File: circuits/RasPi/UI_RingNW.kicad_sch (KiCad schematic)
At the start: 11 parts, among them SW2 SW_DIP_x04, SW3 SW_SPDT

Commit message: ラズパイ基板とか
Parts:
- R4, R5: value 2k -> 1k
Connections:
- net DIP_SW0 renamed DIPSW0
- net DIP_SW1 renamed DIPSW1
- net DIP_SW2 renamed DIPSW2
- net DIP_SW3 renamed DIPSW3
- net Slide_SW0 renamed SlideSW0
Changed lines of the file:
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@@
     (effects (font (size 2.54 2.54)) (justify left bottom))
   )
-  (hierarchical_label "Slide_SW0" (shape input) (at 132.08 78.74 0) (fields_autoplaced)
+  (hierarchical_label "SlideSW0" (shape input) (at 132.08 78.74 0) (fields_autoplaced)
     (effects (font (size 1.27 1.27)) (justify left))
   )
@@
     (effects (font (size 1.27 1.27)) (justify right))
   )
-  (hierarchical_label "DIP_SW3" (shape input) (at 144.78 119.38 0) (fields_autoplaced)
+  (hierarchical_label "DIPSW0" (shape input) (at 144.78 111.76 0) (fields_autoplaced)
+    (effects (font (size 1.27 1.27)) (justify left))
+  )
+  (hierarchical_label "DIPSW1" (shape input) (at 144.78 114.3 0) (fields_autoplaced)
     (effects (font (size 1.27 1.27)) (justify left))
   )
@@
     (effects (font (size 1.27 1.27)) (justify right))
   )
-  (hierarchical_label "DIP_SW0" (shape input) (at 144.78 111.76 0) (fields_autoplaced)
-    (effects (font (size 1.27 1.27)) (justify left))
-  )
-  (hierarchical_label "DIP_SW1" (shape input) (at 144.78 114.3 0) (fields_autoplaced)
-    (effects (font (size 1.27 1.27)) (justify left))
-  )
-  (hierarchical_label "DIP_SW2" (shape input) (at 144.78 116.84 0) (fields_autoplaced)
+  (hierarchical_label "DIPSW3" (shape input) (at 144.78 119.38 0) (fields_autoplaced)
+    (effects (font (size 1.27 1.27)) (justify left))
+  )
+  (hierarchical_label "DIPSW2" (shape input) (at 144.78 116.84 0) (fields_autoplaced)
     (effects (font (size 1.27 1.27)) (justify left))
   )
@@
       (effects (font (size 1.27 1.27)))
     )
-    (property "Value" "2k" (at 124.46 60.96 90)
+    (property "Value" "1k" (at 124.46 60.96 90)
       (effects (font (size 1.27 1.27)))
     )
@@
       (effects (font (size 1.27 1.27)))
     )
-    (property "Value" "2k" (at 124.46 50.8 90)
-      (effects (font (size 1.27 1.27)))
-    )
+    (property "Value" "1k" (at 124.46 50.8 90)
+      (effects (font (size 1.27 1.27)))
+    )

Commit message: PDFプロット
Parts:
- added D20: Red, LED_SMD:LED_0603_1608Metric_Pad1.05x0.95mm_HandSolder, symbol Device:LED
- added D21: LightGreen, LED_SMD:LED_0603_1608Metric_Pad1.05x0.95mm_HandSolder, symbol Device:LED
- added D22: Yellow, LED_SMD:LED_0603_1608Metric_Pad1.05x0.95mm_HandSolder, symbol Device:LED
- added Q29: BSS138, Package_TO_SOT_SMD:SOT-23, symbol Device:Q_NMOS_GSD
- added R105: 10k, Resistor_SMD:R_0402_1005Metric, symbol Device:R
- added R107, R108, R109: 1k, Resistor_SMD:R_0402_1005Metric, symbol Device:R
- D2, D3: value Red -> Blue
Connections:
- net +3.3V: now also R109.1
- net GNDD: now also D20.1 (K), D21.1 (K), D22.1 (K), Q29.2 (S), R105.2
- net LED0 renamed LED_B0
- net LED1 renamed LED_B1
- new net: D20.2 (A), Q29.3 (D), R109.2
- new net: D22.2 (A), R108.1
- new net: D21.2 (A), R107.1
- new net LED_LG0: R107.2
- new net LED_Y0: R108.2
- new net LED_nR0: Q29.1 (G), R105.1
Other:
- note added: "Error"
- note added: "Indicator"
- note added: "Running"
- note added: "not Running"
- moved on the sheet: D2, D3, R10, R4, R5, R6, R7, R8, R9, SW2, SW3

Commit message: シンボル・フットプリントMyLib->TomoshibiLib置き換え
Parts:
- SW3: footprint MyLibrary:SW_Slide_3P_SPDT -> TomoshibiLibrary:SW_Slide_3P_SPDT
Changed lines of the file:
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@@
       (effects (font (size 1.27 1.27)) (justify left))
     )
-    (property "Footprint" "MyLibrary:SW_Slide_3P_SPDT" (at 121.92 86.36 0)
+    (property "Footprint" "TomoshibiLibrary:SW_Slide_3P_SPDT" (at 121.92 86.36 0)
       (effects (font (size 1.27 1.27)) hide)
     )

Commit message: 更新
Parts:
- removed Q29: BSS138, Package_TO_SOT_SMD:SOT-23, symbol Device:Q_NMOS_GSD
- added Q10: 2N7002, Package_TO_SOT_SMD:SOT-23, symbol Transistor_FET:2N7002
- SW3: footprint TomoshibiLibrary:SW_Slide_3P_SPDT -> TomoshibiLibrary:SW_Slide_SPDT_SSSS213202
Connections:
- net GNDD: now also Q10.2 (S)
- net LED_nR0: now also Q10.1 (G)
- net at D20.2 (A), R109.2: now also Q10.3 (D)
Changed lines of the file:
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@@
 (kicad_sch (version 20230121) (generator eeschema)
   (paper "A4")
+  (junction (at 195.58 86.36) (diameter 0) (color 0 0 0 0)
+  )
   (junction (at 142.24 132.08) (diameter 0) (color 0 0 0 0)
   )
@@
   )
   (junction (at 127 114.3) (diameter 0) (color 0 0 0 0)
-  )
-  (junction (at 195.58 86.36) (diameter 0) (color 0 0 0 0)
   )
   (no_connect (at 127 83.82))
@@
     )
   )
+  (symbol (lib_id "Transistor_FET:2N7002") (at 200.66 86.36 0) (unit 1)
+    (in_bom yes) (on_board yes) (dnp no)
+    (property "Reference" "Q10" (at 193.04 78.74 0)
+      (effects (font (size 1.27 1.27)) (justify left))
+    )
+    (property "Value" "2N7002" (at 193.04 81.28 0)
+      (effects (font (size 1.27 1.27)) (justify left))
+    )
+    (property "Footprint" "Package_TO_SOT_SMD:SOT-23" (at 205.74 88.265 0)
+      (effects (font (size 1.27 1.27) italic) (justify left) hide)
+    )
+    (property "Datasheet" "https://www.onsemi.com/pub/Collateral/NDS7002A-D.PDF" (at 205.74 90.17 0)
+      (effects (font (size 1.27 1.27)) (justify left) hide)
+    )
+    (pin "3")
+    (pin "1")
+    (pin "2")
+    (instances
+      (project "RasPi"
+        (path "/689a9e74-f202-4ea4-bfbb-4341f2549250/24ae560a-4b26-4668-af95-4f511f2fb172/2e4c9748-adeb-4e60-9765-444b8aabd502"
+          (reference "Q10") (unit 1)
+        )
+      )
+    )
+  )
   (symbol (lib_id "power:GNDD") (at 215.9 114.3 0) (unit 1)
     (in_bom yes) (on_board yes) (dnp no) (fields_autoplaced)
@@
         (path "/689a9e74-f202-4ea4-bfbb-4341f2549250/24ae560a-4b26-4668-af95-4f511f2fb172/2e4c9748-adeb-4e60-9765-444b8aabd502"
           (reference "#PWR0140") (unit 1)
+        )
+      )
+    )
+  )
+  (symbol (lib_id "Switch:SW_SPDT") (at 121.92 86.36 0) (mirror x) (unit 1)
+    (in_bom yes) (on_board yes) (dnp no)
+    (property "Reference" "SW3" (at 114.3 93.7514 0)
+      (effects (font (size 1.27 1.27)) (justify left))
+    )
+    (property "Value" "SW_SPDT" (at 114.3 91.44 0)
+      (effects (font (size 1.27 1.27)) (justify left))
+    )
+    (property "Footprint" "TomoshibiLibrary:SW_Slide_SPDT_SSSS213202" (at 121.92 86.36 0)
+      (effects (font (size 1.27 1.27)) hide)
+    )
+    (property "Datasheet" "~" (at 121.92 86.36 0)
+      (effects (font (size 1.27 1.27)) hide)
+    )
+    (pin "1")
+    (pin "2")
+    (pin "3")
+    (instances
+      (project "RasPi"
+        (path "/689a9e74-f202-4ea4-bfbb-4341f2549250/24ae560a-4b26-4668-af95-4f511f2fb172/2e4c9748-adeb-4e60-9765-444b8aabd502"
+          (reference "SW3") (unit 1)
         )
       )
@@
     )
   )
-  (symbol (lib_id "Switch:SW_SPDT") (at 121.92 86.36 0) (mirror x) (unit 1)
-    (in_bom yes) (on_board yes) (dnp no)
-    (property "Reference" "SW3" (at 114.3 93.7514 0)
-      (effects (font (size 1.27 1.27)) (justify left))
-    )
-    (property "Value" "SW_SPDT" (at 114.3 91.44 0)
-      (effects (font (size 1.27 1.27)) (justify left))
-    )
-    (property "Footprint" "TomoshibiLibrary:SW_Slide_3P_SPDT" (at 121.92 86.36 0)
-      (effects (font (size 1.27 1.27)) hide)
-    )
-    (property "Datasheet" "~" (at 121.92 86.36 0)
-      (effects (font (size 1.27 1.27)) hide)
-    )
-    (pin "1")
-    (pin "2")
-    (pin "3")
-    (instances
-      (project "RasPi"
-        (path "/689a9e74-f202-4ea4-bfbb-4341f2549250/24ae560a-4b26-4668-af95-4f511f2fb172/2e4c9748-adeb-4e60-9765-444b8aabd502"
-          (reference "SW3") (unit 1)
-        )
-      )
-    )
-  )
   (symbol (lib_id "Device:R") (at 210.82 76.2 0) (mirror y) (unit 1)
     (in_bom yes) (on_board yes) (dnp no)
@@
         )
       )
-    )
-  )
-  (symbol (lib_name "Q_NMOS_GSD_1") (lib_id "Device:Q_NMOS_GSD") (at 200.66 86.36 0) (unit 1)
-    (in_bom yes) (on_board yes) (dnp no)
-    (property "Reference" "Q29" (at 198.12 91.44 0)
-      (effects (font (size 1.27 1.27)) (justify left))
-    )
-    (property "Value" "BSS138" (at 198.12 93.98 0)
-      (effects (font (size 1.27 1.27)) (justify left))
-    )
-    (property "Footprint" "Package_TO_SOT_SMD:SOT-23" (at 205.74 83.82 0)
-      (effects (font (size 1.27 1.27)) hide)
-    )
-    (property "Datasheet" "~" (at 200.66 86.36 0)
-      (effects (font (size 1.27 1.27)) hide)
-    )
-    (pin "1")
-    (pin "2")
-    (pin "3")
-    (instances
-      (project "RasPi"
-        (path "/689a9e74-f202-4ea4-bfbb-4341f2549250/24ae560a-4b26-4668-af95-4f511f2fb172/2e4c9748-adeb-4e60-9765-444b8aabd502"
-          (reference "Q29") (unit 1)
-        )
-      )

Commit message: raspi基板回路図
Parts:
- added H5, H6: MountingHole_Pad, TestPoint:TestPoint_Pad_1.0x1.0mm, symbol Mechanical:MountingHole_Pad
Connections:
- net LED_B0: now also H5.1
- net LED_B1: now also H6.1
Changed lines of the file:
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@@
   (junction (at 137.16 132.08) (diameter 0) (color 0 0 0 0)
   )
+  (junction (at 119.38 50.8) (diameter 0) (color 0 0 0 0)
+  )
   (junction (at 106.68 119.38) (diameter 0) (color 0 0 0 0)
   )
@@
   )
   (junction (at 129.54 88.9) (diameter 0) (color 0 0 0 0)
+  )
+  (junction (at 119.38 60.96) (diameter 0) (color 0 0 0 0)
   )
   (junction (at 142.24 121.92) (diameter 0) (color 0 0 0 0)
@@
     (stroke (width 0) (type default))
   )
+  (wire (pts (xy 119.38 60.96) (xy 120.65 60.96))
+    (stroke (width 0) (type default))
+  )
   (wire (pts (xy 201.93 50.8) (xy 204.47 50.8))
     (stroke (width 0) (type default))
   )
-  (wire (pts (xy 116.84 60.96) (xy 120.65 60.96))
+  (wire (pts (xy 116.84 60.96) (xy 119.38 60.96))
     (stroke (width 0) (type default))
   )
@@
   (polyline (pts (xy 233.68 124.46) (xy 233.68 40.64))
     (stroke (width 0.5) (type solid))
+  )
+  (wire (pts (xy 119.38 50.8) (xy 120.65 50.8))
+    (stroke (width 0) (type default))
   )
   (polyline (pts (xy 96.52 142.24) (xy 96.52 40.64))
@@
     (stroke (width 0) (type default))
   )
-  (wire (pts (xy 116.84 50.8) (xy 120.65 50.8))
+  (wire (pts (xy 116.84 50.8) (xy 119.38 50.8))
     (stroke (width 0) (type default))
   )
@@
         (path "/689a9e74-f202-4ea4-bfbb-4341f2549250/24ae560a-4b26-4668-af95-4f511f2fb172/2e4c9748-adeb-4e60-9765-444b8aabd502"
           (reference "R10") (unit 1)
+        )
+      )
+    )
+  )
+  (symbol (lib_id "Mechanical:MountingHole_Pad") (at 119.38 58.42 0) (mirror y) (unit 1)
+    (in_bom yes) (on_board yes) (dnp no)
+    (property "Reference" "H6" (at 104.14 55.88 0)
+      (effects (font (size 1.27 1.27)) (justify right))
+    )
+    (property "Value" "MountingHole_Pad" (at 104.14 53.34 0)
+      (effects (font (size 1.27 1.27)) (justify right))
+    )
+    (property "Footprint" "TestPoint:TestPoint_Pad_1.0x1.0mm" (at 119.38 58.42 0)
+      (effects (font (size 1.27 1.27)) hide)
+    )
+    (property "Datasheet" "~" (at 119.38 58.42 0)
+      (effects (font (size 1.27 1.27)) hide)
+    )
+    (pin "1")
+    (instances
+      (project "RasPi"
+        (path "/689a9e74-f202-4ea4-bfbb-4341f2549250/24ae560a-4b26-4668-af95-4f511f2fb172/2e4c9748-adeb-4e60-9765-444b8aabd502"
+          (reference "H6") (unit 1)
         )
       )
@@
         )
       )
+    )
+  )
+  (symbol (lib_id "Mechanical:MountingHole_Pad") (at 119.38 48.26 0) (mirror y) (unit 1)
+    (in_bom yes) (on_board yes) (dnp no)
+    (property "Reference" "H5" (at 104.14 45.72 0)
+      (effects (font (size 1.27 1.27)) (justify right))
+    )
+    (property "Value" "MountingHole_Pad" (at 104.14 43.18 0)
+      (effects (font (size 1.27 1.27)) (justify right))
+    )
+    (property "Footprint" "TestPoint:TestPoint_Pad_1.0x1.0mm" (at 119.38 48.26 0)
+      (effects (font (size 1.27 1.27)) hide)
+    )
+    (property "Datasheet" "~" (at 119.38 48.26 0)
+      (effects (font (size 1.27 1.27)) hide)
+    )
+    (pin "1")
+    (instances
+      (project "RasPi"
+        (path "/689a9e74-f202-4ea4-bfbb-4341f2549250/24ae560a-4b26-4668-af95-4f511f2fb172/2e4c9748-adeb-4e60-9765-444b8aabd502"
+          (reference "H5") (unit 1)
+        )
+      )

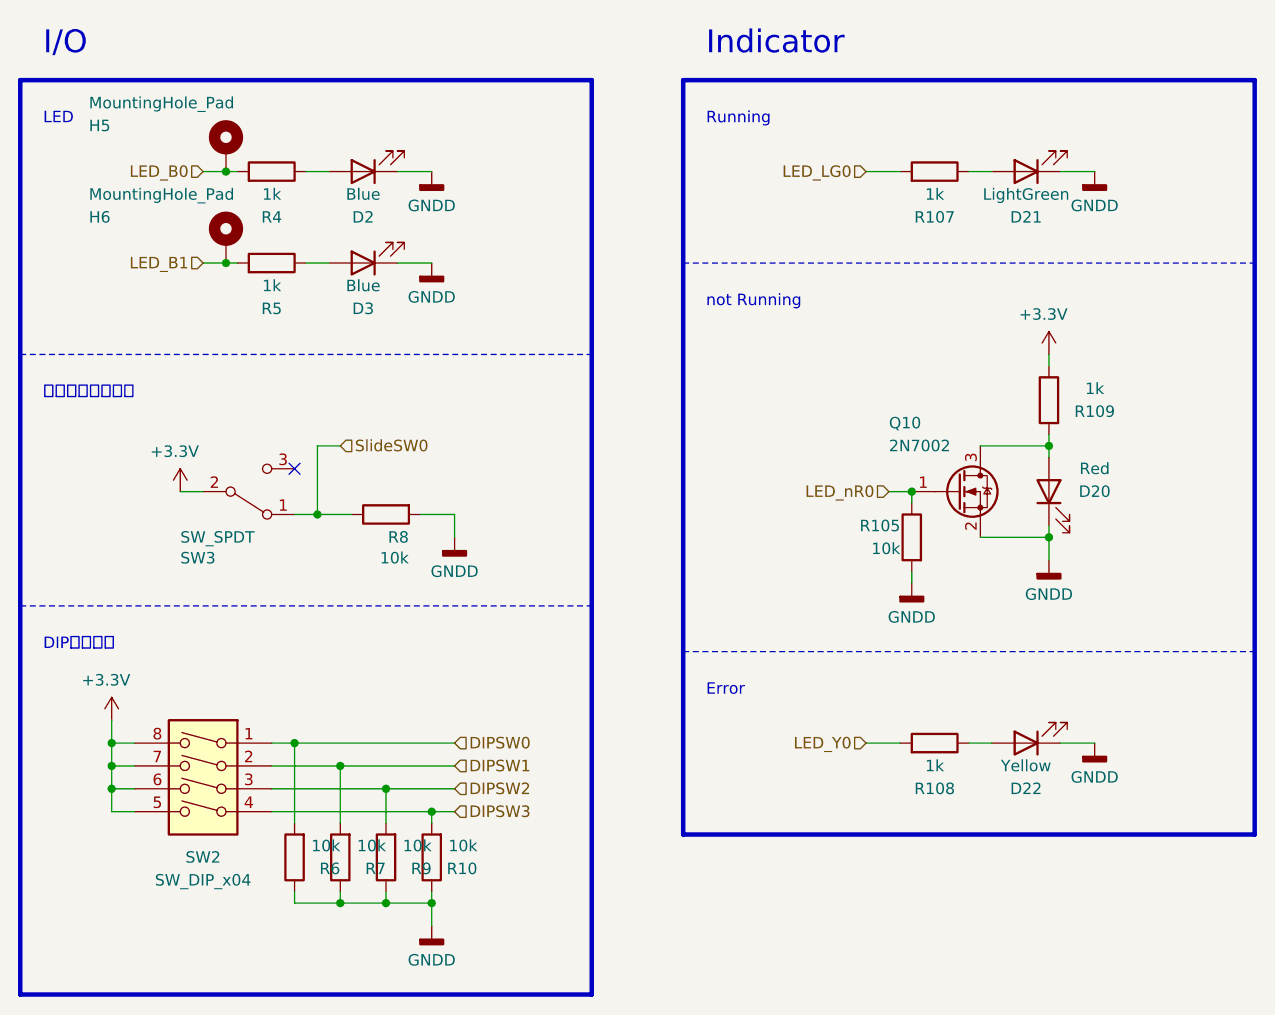
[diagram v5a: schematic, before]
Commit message: 発注第2弾
RasPi発注
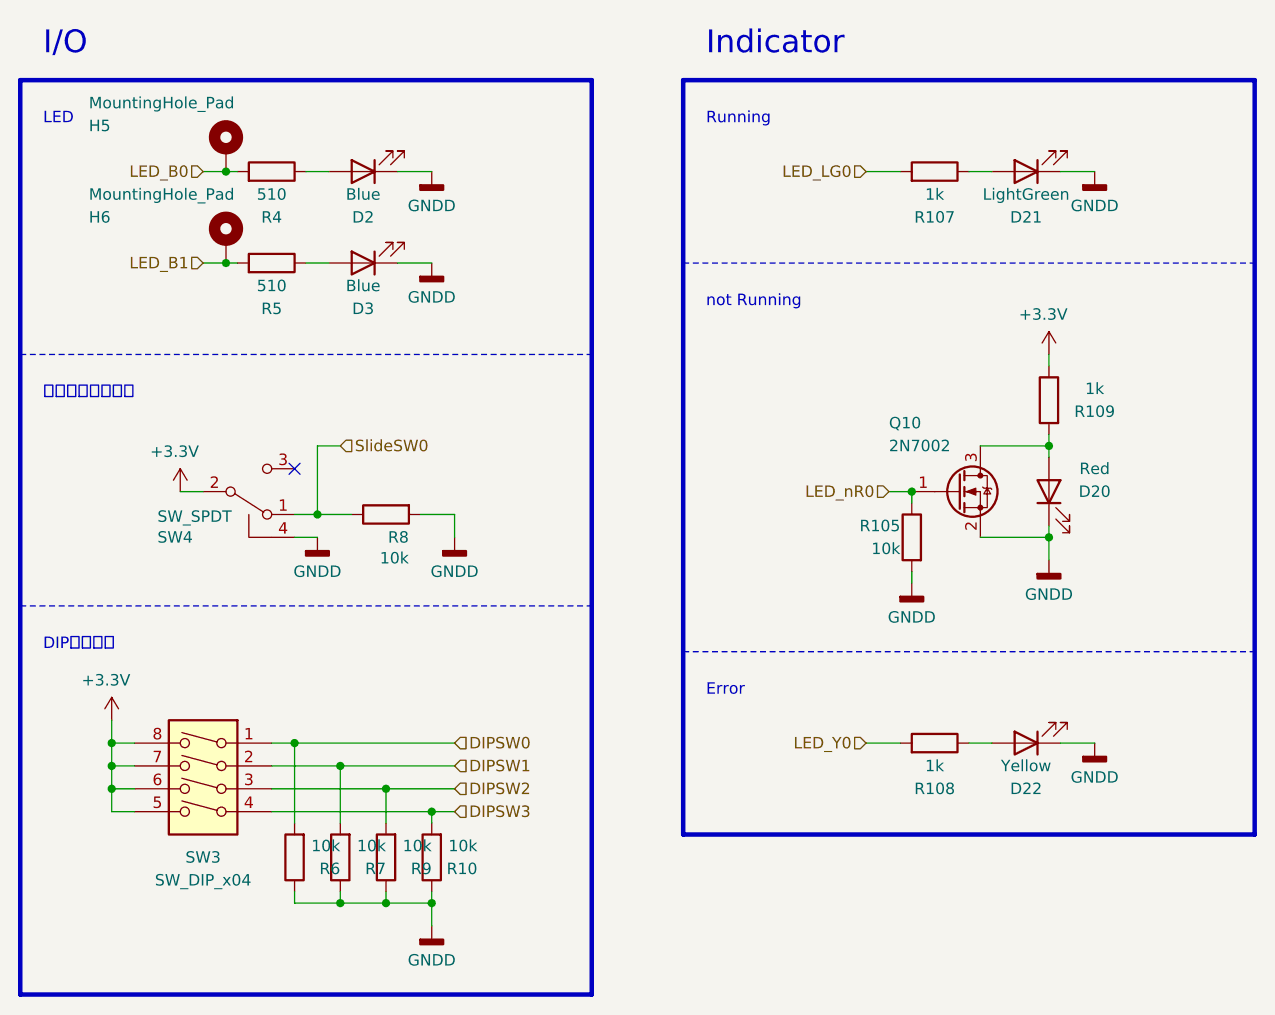
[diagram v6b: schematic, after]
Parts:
- Q10: footprint Package_TO_SOT_SMD:SOT-23 -> Package_TO_SOT_SMD:SC-59
- R4, R5: value 1k -> 510; footprint Resistor_SMD:R_0402_1005Metric -> Resistor_SMD:R_0603_1608Metric
- SW4: renamed from SW3; footprint TomoshibiLibrary:SW_Slide_SPDT_SSSS213202 -> TomoshibiLibrary:SW_Slide_DPDT_SSSS820101
- renumbered SW2 to SW3
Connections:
- net GNDD: now also SW4.4, SW4.5 (shell), SW4.6 (shell), SW4.G1 (shell), SW4.G2 (shell), SW4.G3 (shell), SW4.G4 (shell)
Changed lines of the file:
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@@
+    (stroke (width 0) (type default))
+  )
+  (wire (pts (xy 127 91.44) (xy 129.54 91.44))
     (stroke (width 0) (type default))
   )
@@
       (effects (font (size 1.27 1.27)))
     )
-    (property "Value" "1k" (at 124.46 63.5 90)
-      (effects (font (size 1.27 1.27)))
-    )
-    (property "Footprint" "Resistor_SMD:R_0402_1005Metric" (at 124.46 62.738 90)
+    (property "Value" "510" (at 124.46 63.5 90)
+      (effects (font (size 1.27 1.27)))
+    )
+    (property "Footprint" "Resistor_SMD:R_0603_1608Metric" (at 124.46 62.738 90)
       (effects (font (size 1.27 1.27)) hide)
     )
@@
       (effects (font (size 1.27 1.27)) (justify left))
     )
-    (property "Footprint" "Package_TO_SOT_SMD:SOT-23" (at 205.74 88.265 0)
+    (property "Footprint" "Package_TO_SOT_SMD:SC-59" (at 205.74 88.265 0)
       (effects (font (size 1.27 1.27) italic) (justify left) hide)
     )
@@
     )
   )
-  (symbol (lib_id "Switch:SW_SPDT") (at 121.92 86.36 0) (mirror x) (unit 1)
-    (in_bom yes) (on_board yes) (dnp no)
-    (property "Reference" "SW3" (at 114.3 93.7514 0)
-      (effects (font (size 1.27 1.27)) (justify left))
-    )
-    (property "Value" "SW_SPDT" (at 114.3 91.44 0)
-      (effects (font (size 1.27 1.27)) (justify left))
-    )
-    (property "Footprint" "TomoshibiLibrary:SW_Slide_SPDT_SSSS213202" (at 121.92 86.36 0)
+  (symbol (lib_id "power:GNDD") (at 129.54 91.44 0) (unit 1)
+    (in_bom yes) (on_board yes) (dnp no) (fields_autoplaced)
+    (property "Reference" "#PWR0152" (at 129.54 97.79 0)
+      (effects (font (size 1.27 1.27)) hide)
+    )
+    (property "Value" "GNDD" (at 129.54 95.25 0)
+      (effects (font (size 1.27 1.27)))
+    )
+    (property "Footprint" "" (at 129.54 91.44 0)
+      (effects (font (size 1.27 1.27)) hide)
+    )
+    (property "Datasheet" "" (at 129.54 91.44 0)
+      (effects (font (size 1.27 1.27)) hide)
+    )
+    (pin "1")
+    (instances
+      (project "RasPi"
+        (path "/689a9e74-f202-4ea4-bfbb-4341f2549250/24ae560a-4b26-4668-af95-4f511f2fb172/2e4c9748-adeb-4e60-9765-444b8aabd502"
+          (reference "#PWR0152") (unit 1)
+        )
+      )
+    )
+  )
+  (symbol (lib_name "SW_SPDT_1") (lib_id "Switch:SW_SPDT") (at 121.92 86.36 0) (mirror x) (unit 1)
+    (in_bom yes) (on_board yes) (dnp no)
+    (property "Reference" "SW4" (at 111.76 91.44 0)
+      (effects (font (size 1.27 1.27)) (justify left))
+    )
+    (property "Value" "SW_SPDT" (at 111.76 89.1286 0)
+      (effects (font (size 1.27 1.27)) (justify left))
+    )
+    (property "Footprint" "TomoshibiLibrary:SW_Slide_DPDT_SSSS820101" (at 121.92 86.36 0)
       (effects (font (size 1.27 1.27)) hide)
     )
@@
     (pin "2")
     (pin "3")
-    (instances
-      (project "RasPi"
-        (path "/689a9e74-f202-4ea4-bfbb-4341f2549250/24ae560a-4b26-4668-af95-4f511f2fb172/2e4c9748-adeb-4e60-9765-444b8aabd502"
-          (reference "SW3") (unit 1)
+    (pin "4")
+    (pin "5")
+    (pin "G1")
+    (pin "6")
+    (pin "G2")
+    (pin "G4")
+    (pin "G3")
+    (instances
+      (project "RasPi"
+        (path "/689a9e74-f202-4ea4-bfbb-4341f2549250/24ae560a-4b26-4668-af95-4f511f2fb172/2e4c9748-adeb-4e60-9765-444b8aabd502"
+          (reference "SW4") (unit 1)
         )
       )
@@
   (symbol (lib_id "Switch:SW_DIP_x04") (at 116.84 119.38 0) (mirror y) (unit 1)
     (in_bom yes) (on_board yes) (dnp no)
-    (property "Reference" "SW2" (at 116.84 127 0)
+    (property "Reference" "SW3" (at 116.84 127 0)
       (effects (font (size 1.27 1.27)))
     )
@@
       (project "RasPi"
         (path "/689a9e74-f202-4ea4-bfbb-4341f2549250/24ae560a-4b26-4668-af95-4f511f2fb172/2e4c9748-adeb-4e60-9765-444b8aabd502"
-          (reference "SW2") (unit 1)
+          (reference "SW3") (unit 1)
         )
       )
@@
       (effects (font (size 1.27 1.27)))
     )
-    (property "Value" "1k" (at 124.46 53.34 90)
-      (effects (font (size 1.27 1.27)))
-    )
-    (property "Footprint" "Resistor_SMD:R_0402_1005Metric" (at 124.46 52.578 90)
-      (effects (font (size 1.27 1.27)) hide)
-    )
+    (property "Value" "510" (at 124.46 53.34 90)
+      (effects (font (size 1.27 1.27)))
+    )
+    (property "Footprint" "Resistor_SMD:R_0603_1608Metric" (at 124.46 52.578 90)
+      (effects (font (size 1.27 1.27)) hide)
+    )
